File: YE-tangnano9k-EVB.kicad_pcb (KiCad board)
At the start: 2 copper layers, 95 x 72 mm, 27 parts, among them J1 Conn_01x24_Socket, J2 Conn_01x24_Socket, Q1 2SC1815, SW1 SW_SPDT, SW2 SW_Push, SW3 SW_Push, SW4 SW_Push, SW5 SW_Push, SW6 SW_Push, U1 Tang Nano 9K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

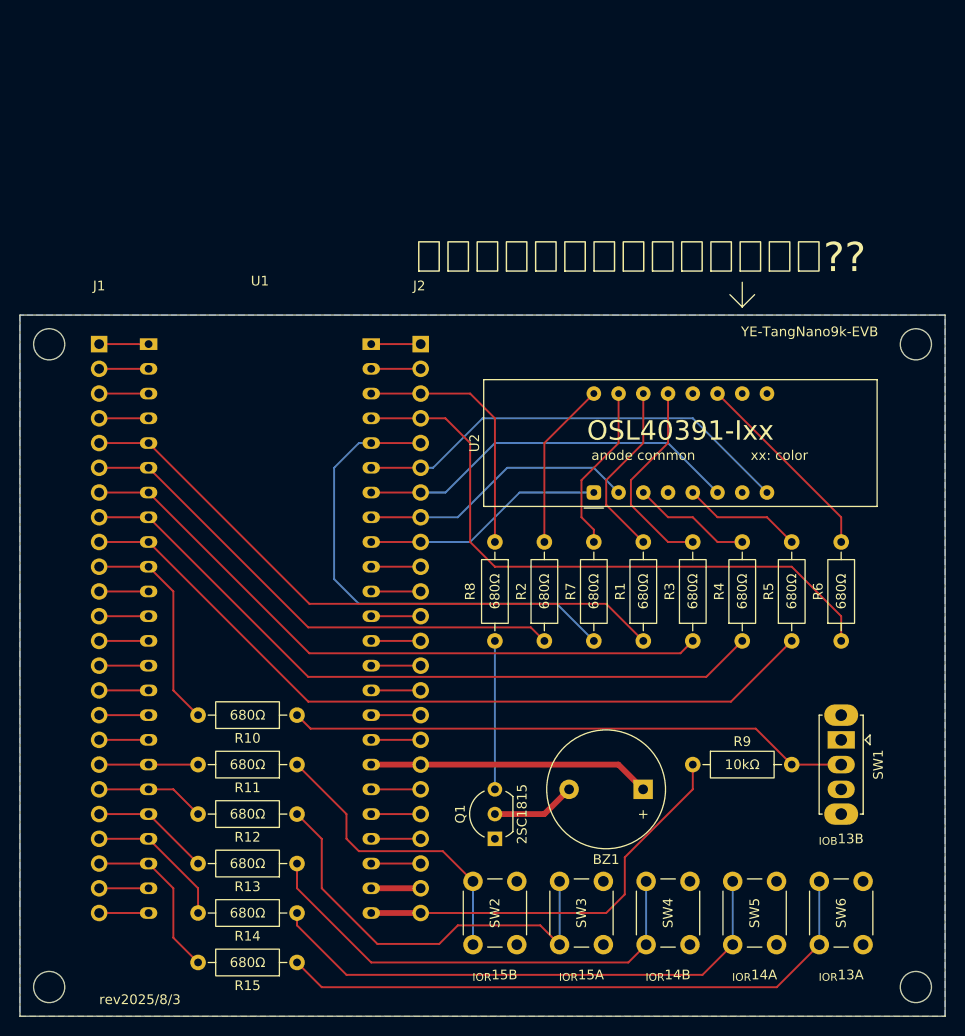
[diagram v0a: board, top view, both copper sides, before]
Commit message: add yasushi_icon fix Front_silk
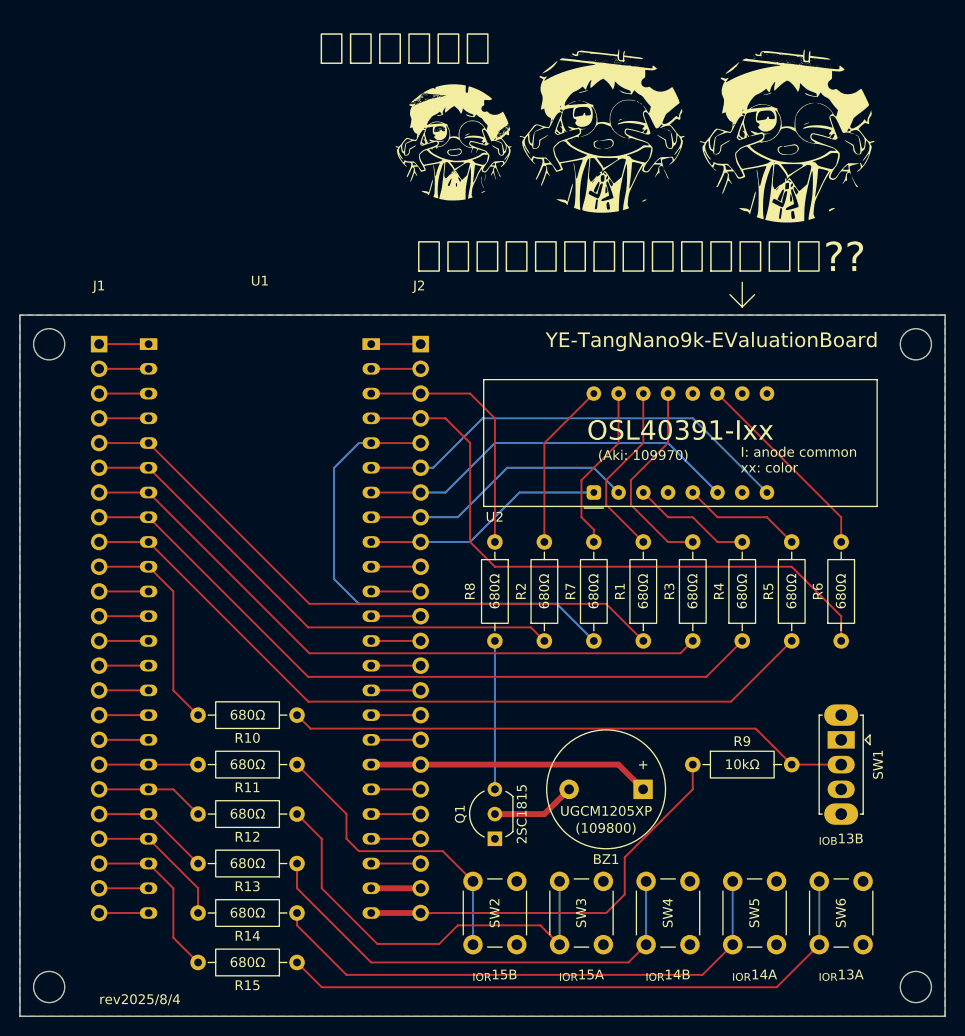
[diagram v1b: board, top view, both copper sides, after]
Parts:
- added G***: LOGO, LOGO, F.Cu at (12.2, -55.0)
- added G***: LOGO, LOGO, F.Cu at (-3.00, -53.8)
- added G***: LOGO, LOGO, F.Cu at (31.2, -54.5)
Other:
- board text added: "(Aki: 109970)"
- board text added: "I: anode common xx: color"
- board text added: "YE-TangNano9k-EValuationBoard"
- board text added: "rev2025/8/4"
- board text added: "アイコン素材"
- board text removed: "YE-TangNano9k-EVB"
- board text removed: "anode common"
- board text removed: "rev2025/8/3"
- board text removed: "xx: color"

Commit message: fix net_name
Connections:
- net /BUZZ renamed /bz
- net /DIG1 renamed /com_1
- net /DIG2 renamed /com_2
- net /DIG3 renamed /com_3
- net /DIG4 renamed /com_4
- net /LED_A renamed /seg_a
- net /LED_B renamed /seg_b
- net /LED_C renamed /seg_c
- net /LED_D renamed /seg_d
- net /LED_E renamed /seg_e
- net /LED_F renamed /seg_f
- net /LED_G renamed /seg_g
- net /Push1 renamed /Push_1
- net /Push2 renamed /Push_2
- net /Push3 renamed /Push_3
- net /Push4 renamed /Push_4
- net /Push5 renamed /Push_5
- net /SW_IN renamed /SYS_EN
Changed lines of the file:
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@@
 	(net 3 "Net-(J1-Pin_15)")
 	(net 4 "Net-(J1-Pin_16)")
-	(net 5 "/Push3")
-	(net 6 "/LED_B")
-	(net 7 "/LED_A")
+	(net 5 "/Push_3")
+	(net 6 "/seg_b")
+	(net 7 "/seg_a")
 	(net 8 "Net-(J1-Pin_13)")
-	(net 9 "/Push1")
+	(net 9 "/Push_1")
 	(net 10 "Net-(J1-Pin_3)")
-	(net 11 "/LED_E")
-	(net 12 "/LED_D")
-	(net 13 "/LED_C")
+	(net 11 "/seg_e")
+	(net 12 "/seg_d")
+	(net 13 "/seg_c")
 	(net 14 "Net-(J1-Pin_14)")
 	(net 15 "Net-(J1-Pin_2)")
 	(net 16 "Net-(J1-Pin_12)")
-	(net 17 "/Push4")
+	(net 17 "/Push_4")
 	(net 18 "Net-(J1-Pin_11)")
-	(net 19 "/Push5")
-	(net 20 "/SW_IN")
+	(net 19 "/Push_5")
+	(net 20 "/SYS_EN")
 	(net 21 "Net-(J1-Pin_17)")
 	(net 22 "Net-(J1-Pin_23)")
-	(net 23 "/Push2")
+	(net 23 "/Push_2")
 	(net 24 "Net-(J1-Pin_24)")
 	(net 25 "Net-(J1-Pin_4)")
@@
 	(net 27 "Net-(J2-Pin_11)")
 	(net 28 "GND")
-	(net 29 "/DIG3")
-	(net 30 "/DIG4")
-	(net 31 "/BUZZ")
+	(net 29 "/com_3")
+	(net 30 "/com_4")
+	(net 31 "/bz")
 	(net 32 "Net-(J2-Pin_21)")
 	(net 33 "Net-(J2-Pin_17)")
 	(net 34 "Net-(J2-Pin_15)")
 	(net 35 "Net-(J2-Pin_12)")
-	(net 36 "/DIG1")
+	(net 36 "/com_1")
 	(net 37 "Net-(J2-Pin_22)")
 	(net 38 "Net-(J2-Pin_2)")
@@
 	(net 41 "+3V3")
 	(net 42 "Net-(J2-Pin_10)")
-	(net 43 "/DIG2")
+	(net 43 "/com_2")
 	(net 44 "Net-(J2-Pin_13)")
-	(net 45 "/LED_F")
+	(net 45 "/seg_f")
 	(net 46 "Net-(J2-Pin_19)")
 	(net 47 "Net-(J2-Pin_16)")
-	(net 48 "/LED_G")
+	(net 48 "/seg_g")
 	(net 49 "Net-(J2-Pin_14)")
 	(net 50 "Net-(Q1-B)")
@@
 			(layers "*.Cu" "*.Mask")
 			(remove_unused_layers no)
-			(net 6 "/LED_B")
+			(net 6 "/seg_b")
 			(pintype "passive")
 		)
@@
 			(layers "*.Cu" "*.Mask")
 			(remove_unused_layers no)
-			(net 31 "/BUZZ")
+			(net 31 "/bz")
 			(pintype "passive")
 		)
@@
 			(layers "*.Cu" "*.Mask")
 			(remove_unused_layers no)
-			(net 20 "/SW_IN")
+			(net 20 "/SYS_EN")
 			(pintype "passive")
 		)
@@
 			(layers "*.Cu" "*.Mask")
 			(remove_unused_layers no)
-			(net 7 "/LED_A")
+			(net 7 "/seg_a")
 			(pintype "passive")
 		)
@@
 			(layers "*.Cu" "*.Mask")
 			(remove_unused_layers no)
-			(net 19 "/Push5")
+			(net 19 "/Push_5")
 			(pintype "passive")
 		)
@@
 			(layers "*.Cu" "*.Mask")
 			(remove_unused_layers no)
-			(net 12 "/LED_D")
+			(net 12 "/seg_d")
 			(pintype "passive")
 		)
@@
 			(layers "*.Cu" "*.Mask")
 			(remove_unused_layers no)
-			(net 45 "/LED_F")
+			(net 45 "/seg_f")
 			(pintype "passive")
 		)
@@
 			(layers "*.Cu" "*.Mask")
 			(remove_unused_layers no)
-			(net 13 "/LED_C")
+			(net 13 "/seg_c")
 			(pintype "passive")
 		)
@@
 			(layers "*.Cu" "*.Mask")
 			(remove_unused_layers no)
-			(net 11 "/LED_E")
+			(net 11 "/seg_e")
 			(pintype "passive")
 		)
@@
 			(layers "*.Cu" "*.Mask")
 			(remove_unused_layers no)
-			(net 23 "/Push2")
+			(net 23 "/Push_2")
 			(pintype "passive")
 		)
@@
 			(layers "*.Cu" "*.Mask")
 			(remove_unused_layers no)
-			(net 7 "/LED_A")
+			(net 7 "/seg_a")
 			(pinfunction "PIN25_IOB8A")
 			(pintype "passive")
@@
 			(layers "*.Cu" "*.Mask")
 			(remove_unused_layers no)
-			(net 6 "/LED_B")
+			(net 6 "/seg_b")
 			(pinfunction "PIN26_IOB8B")
 			(pintype "passive")
@@
 			(layers "*.Cu" "*.Mask")
 			(remove_unused_layers no)
-			(net 13 "/LED_C")
+			(net 13 "/seg_c")
 			(pinfunction "PIN27_IOB11A")
 			(pintype "passive")
@@
 			(layers "*.Cu" "*.Mask")
 			(remove_unused_layers no)
-			(net 12 "/LED_D")
+			(net 12 "/seg_d")
 			(pinfunction "PIN28_IOB11B")
 			(pintype "passive")
@@
 			(layers "*.Cu" "*.Mask")
 			(remove_unused_layers no)
-			(net 11 "/LED_E")
+			(net 11 "/seg_e")
 			(pinfunction "PIN29_IOB13A")
 			(pintype "passive")
@@
 			(layers "*.Cu" "*.Mask")
 			(remove_unused_layers no)
-			(net 20 "/SW_IN")
+			(net 20 "/SYS_EN")
 			(pinfunction "PIN30_IOB13B")
 			(pintype "passive")
@@
 			(layers "*.Cu" "*.Mask")
 			(remove_unused_layers no)
-			(net 9 "/Push1")
+			(net 9 "/Push_1")
 			(pinfunction "PIN53_IOR15B_RGB_B4")
 			(pintype "passive")
@@
 			(layers "*.Cu" "*.Mask")
 			(remove_unused_layers no)
-			(net 23 "/Push2")
+			(net 23 "/Push_2")
 			(pinfunction "PIN54_IOR15A_RGB_B3")
 			(pintype "passive")
@@
 			(layers "*.Cu" "*.Mask")
 			(remove_unused_layers no)
-			(net 5 "/Push3")
+			(net 5 "/Push_3")
 			(pinfunction "PIN55_IOR14B_RGB_G7")
 			(pintype "passive")
@@
 			(layers "*.Cu" "*.Mask")
 			(remove_unused_layers no)
-			(net 17 "/Push4")
+			(net 17 "/Push_4")
 			(pinfunction "PIN56_IOR14A_RGB_G6")
 			(pintype "passive")
@@
 			(layers "*.Cu" "*.Mask")
 			(remove_unused_layers no)
-			(net 19 "/Push5")
+			(net 19 "/Push_5")
 			(pinfunction "PIN57_IOR13A_RGB_G5")
 			(pintype "passive")
@@
 			(layers "*.Cu" "*.Mask")
 			(remove_unused_layers no)
-			(net 36 "/DIG1")
+			(net 36 "/com_1")
 			(pinfunction "PIN79_IOT12B_1V8")
 			(pintype "passive")
@@
 			(layers "*.Cu" "*.Mask")
 			(remove_unused_layers no)
-			(net 43 "/DIG2")
+			(net 43 "/com_2")
 			(pinfunction "PIN80_IOT12A_1V8")
 			(pintype "passive")
@@
 			(layers "*.Cu" "*.Mask")
 			(remove_unused_layers no)
-			(net 29 "/DIG3")
+			(net 29 "/com_3")
 			(pinfunction "PIN81_IOT11B_1V8")
 			(pintype "passive")
@@
 			(layers "*.Cu" "*.Mask")
 			(remove_unused_layers no)
-			(net 30 "/DIG4")
+			(net 30 "/com_4")
 			(pinfunction "PIN82_IOT11A_1V8")
 			(pintype "passive")
@@
 			(layers "*.Cu" "*.Mask")
 			(remove_unused_layers no)
-			(net 48 "/LED_G")
+			(net 48 "/seg_g")
 			(pinfunction "PIN83_IOT10B_1V8")
 			(pintype "passive")
@@
 			(layers "*.Cu" "*.Mask")
 			(remove_unused_layers no)
-			(net 45 "/LED_F")
+			(net 45 "/seg_f")
 			(pinfunction "PIN84_IOT10A_1V8")
 			(pintype "passive")
@@
 			(layers "*.Cu" "*.Mask")
 			(remove_unused_layers no)
-			(net 31 "/BUZZ")
+			(net 31 "/bz")
 			(pinfunction "PIN85_IOT8B_1V8")
 			(pintype "passive")
@@
 			(layers "*.Cu" "*.Mask")
 			(remove_unused_layers no)
-			(net 9 "/Push1")
+			(net 9 "/Push_1")
 			(pintype "passive")
 		)
@@
 			(layers "*.Cu" "*.Mask")
 			(remove_unused_layers no)
-			(net 17 "/Push4")
+			(net 17 "/Push_4")
 			(pintype "passive")
 		)
@@
 			(layers "*.Cu" "*.Mask")
 			(remove_unused_layers no)
-			(net 48 "/LED_G")
+			(net 48 "/seg_g")
 			(pintype "passive")
 		)
@@
 			(layers "*.Cu" "*.Mask")
 			(remove_unused_layers no)
-			(net 7 "/LED_A")
+			(net 7 "/seg_a")
 			(pinfunction "Pin_5")
 			(pintype "passive")
@@
 			(layers "*.Cu" "*.Mask")
 			(remove_unused_layers no)
-			(net 6 "/LED_B")
+			(net 6 "/seg_b")
 			(pinfunction "Pin_6")
 			(pintype "passive")
@@
 			(layers "*.Cu" "*.Mask")
 			(remove_unused_layers no)
-			(net 13 "/LED_C")
+			(net 13 "/seg_c")
 			(pinfunction "Pin_7")
 			(pintype "passive")
@@
 			(layers "*.Cu" "*.Mask")
 			(remove_unused_layers no)
-			(net 12 "/LED_D")
+			(net 12 "/seg_d")
 			(pinfunction "Pin_8")
 			(pintype "passive")
@@
 			(layers "*.Cu" "*.Mask")
 			(remove_unused_layers no)
-			(net 11 "/LED_E")
+			(net 11 "/seg_e")
 			(pinfunction "Pin_9")
 			(pintype "passive")
@@
 			(layers "*.Cu" "*.Mask")
 			(remove_unused_layers no)
-			(net 20 "/SW_IN")
+			(net 20 "/SYS_EN")
 			(pinfunction "Pin_10")
 			(pintype "passive")
@@
 			(layers "*.Cu" "*.Mask")
 			(remove_unused_layers no)
-			(net 9 "/Push1")
+			(net 9 "/Push_1")
 			(pinfunction "Pin_18")
 			(pintype "passive")
@@
 			(layers "*.Cu" "*.Mask")
 			(remove_unused_layers no)
-			(net 23 "/Push2")
+			(net 23 "/Push_2")
 			(pinfunction "Pin_19")
 			(pintype "passive")
@@
 			(layers "*.Cu" "*.Mask")
 			(remove_unused_layers no)
-			(net 5 "/Push3")
+			(net 5 "/Push_3")
 			(pinfunction "Pin_20")
 			(pintype "passive")
@@
 			(layers "*.Cu" "*.Mask")
 			(remove_unused_layers no)
-			(net 17 "/Push4")
+			(net 17 "/Push_4")
 			(pinfunction "Pin_21")
 			(pintype "passive")
@@
 			(layers "*.Cu" "*.Mask")
 			(remove_unused_layers no)
-			(net 19 "/Push5")
+			(net 19 "/Push_5")
 			(pinfunction "Pin_22")
 			(pintype "passive")
@@
 			(remove_unused_layers no)
 			(roundrect_rratio 0.25)
-			(net 36 "/DIG1")
+			(net 36 "/com_1")
 			(pinfunction "CA1")
 			(pintype "input")
@@
 			(layers "*.Cu" "*.Mask")
 			(remove_unused_layers no)
-			(net 43 "/DIG2")
+			(net 43 "/com_2")
 			(pinfunction "CA2")
 			(pintype "input")
@@
 			(layers "*.Cu" "*.Mask")
 			(remove_unused_layers no)
-			(net 29 "/DIG3")
+			(net 29 "/com_3")
 			(pinfunction "CA3")
 			(pintype "input")
@@
 			(layers "*.Cu" "*.Mask")
 			(remove_unused_layers no)
-			(net 30 "/DIG4")
+			(net 30 "/com_4")
 			(pinfunction "CA4")
 			(pintype "input")
@@
 			(layers "*.Cu" "*.Mask")
 			(remove_unused_layers no)
-			(net 5 "/Push3")
+			(net 5 "/Push_3")
 			(pintype "passive")
 		)
@@
 			(layers "*.Cu" "*.Mask")
 			(remove_unused_layers no)
-			(net 31 "/BUZZ")
+			(net 31 "/bz")
 			(pinfunction "Pin_3")
 			(pintype "passive")
@@
 			(layers "*.Cu" "*.Mask")
 			(remove_unused_layers no)
-			(net 45 "/LED_F")
+			(net 45 "/seg_f")
 			(pinfunction "Pin_4")
 			(pintype "passive")
@@
 			(layers "*.Cu" "*.Mask")
 			(remove_unused_layers no)
-			(net 48 "/LED_G")
+			(net 48 "/seg_g")
 			(pinfunction "Pin_5")
 			(pintype "passive")
@@
 			(layers "*.Cu" "*.Mask")
 			(remove_unused_layers no)
-			(net 30 "/DIG4")
+			(net 30 "/com_4")
 			(pinfunction "Pin_6")
 			(pintype "passive")
@@
 			(layers "*.Cu" "*.Mask")
 			(remove_unused_layers no)
-			(net 29 "/DIG3")
+			(net 29 "/com_3")
 			(pinfunction "Pin_7")
 			(pintype "passive")
@@
 			(layers "*.Cu" "*.Mask")
 			(remove_unused_layers no)
-			(net 43 "/DIG2")
+			(net 43 "/com_2")
 			(pinfunction "Pin_8")
 			(pintype "passive")
@@
 			(layers "*.Cu" "*.Mask")
 			(remove_unused_layers no)
-			(net 36 "/DIG1")
+			(net 36 "/com_1")
 			(pinfunction "Pin_9")
 			(pintype "passive")

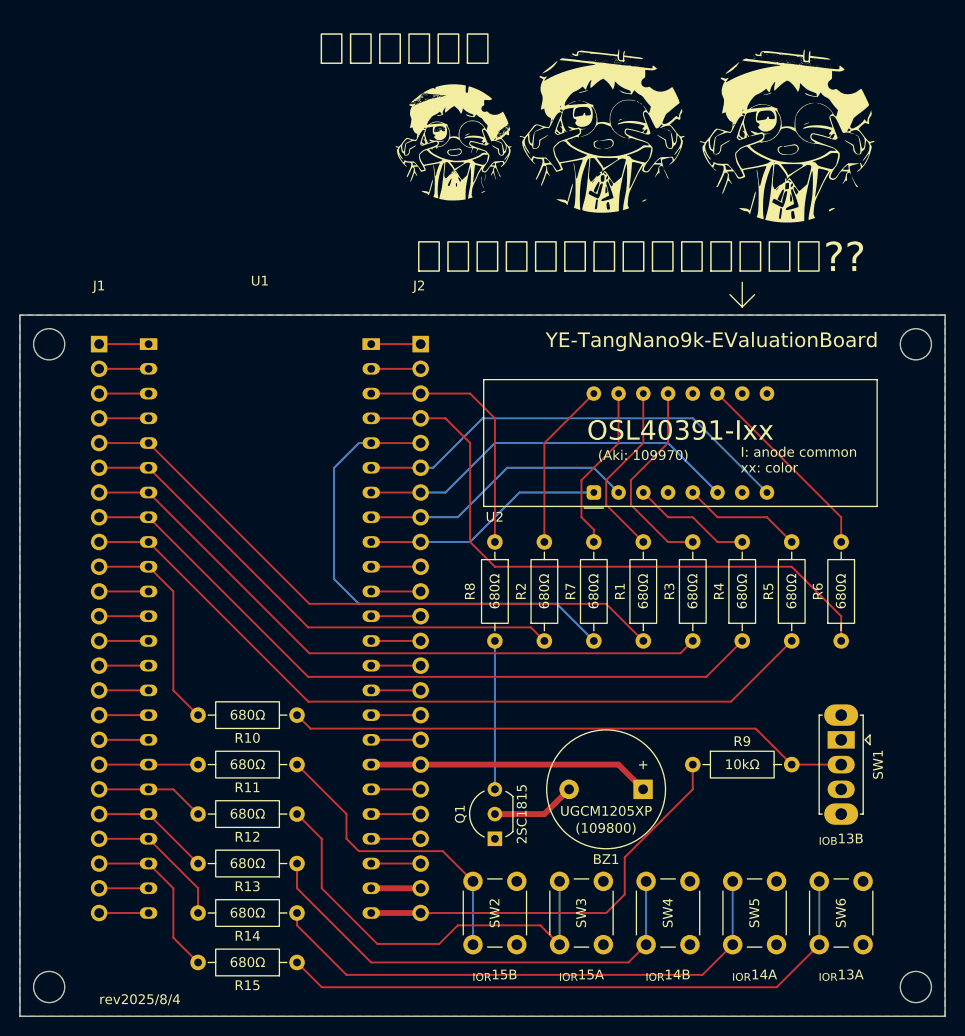
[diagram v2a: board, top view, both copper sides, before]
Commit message: change pushSW net change buzzer logic(ActiveHigh → ActiveLow)
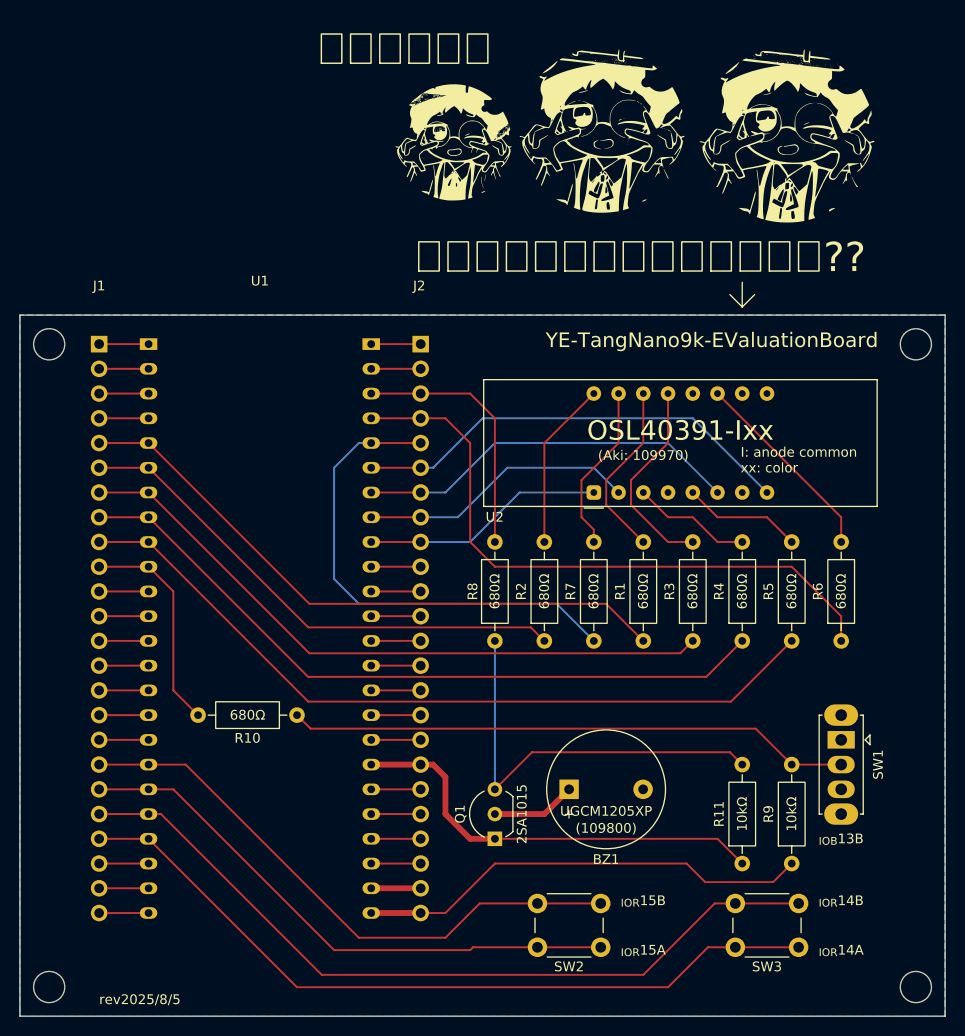
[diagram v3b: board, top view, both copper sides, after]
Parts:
- removed R12, R13, R14, R15: 680, Resistor_THT:R_Axial_DIN0207_L6.3mm_D2.5mm_P10.16mm_Horizontal
- removed SW4, SW5, SW6: SW_Push, Button_Switch_THT:SW_PUSH_6mm_H7.3mm
- Q1: value 2SC1815 -> 2SA1015
- R11: value 680 -> 10k
- moved R11 46.8 mm to (26.7, 20.3), turned to 90 degrees
- moved R9 14.4 mm to (31.8, 20.3), turned to 90 degrees
- moved SW3 13.7 mm to (26.0, 24.4), turned to 0 degrees
- moved R8 10.2 mm to (1.27, -2.54), turned to 90 degrees
- moved BZ1 7.60 mm to (8.89, 12.7), turned to 0 degrees
- moved SW2 3.11 mm to (5.64, 24.4), turned to 0 degrees
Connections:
- net /Push_5 renamed Net-(J1-Pin_22)
- BZ1 pad 1: +5V -> Net-(BZ1-+)
- BZ1 pad 2: Net-(BZ1--) -> GND
- J1 pad 18: /Push_1 -> /IOR15B
- J1 pad 19: /Push_2 -> /IOR15A
- J1 pad 20: /Push_3 -> /IOR14B
- J1 pad 21: /Push_4 -> /IOR14A
- Q1 pad 1: GND -> +5V
- Q1 pad 2: Net-(BZ1--) -> Net-(BZ1-+)
- R11 pad 1: Net-(R11-Pad1) -> +5V
- R11 pad 2: /Push_1 -> Net-(Q1-B)
- R8 pad 1: /bz -> Net-(Q1-B)
- R8 pad 2: Net-(Q1-B) -> /bz
- SW2 pad 1: GND -> /IOR15B
- SW2 pad 2: Net-(R11-Pad1) -> /IOR15A
- SW3 pad 1: GND -> /IOR14B
- SW3 pad 2: Net-(R12-Pad1) -> /IOR14A
- U1 pad 18: /Push_1 -> /IOR15B
- U1 pad 19: /Push_2 -> /IOR15A
- U1 pad 20: /Push_3 -> /IOR14B
- U1 pad 21: /Push_4 -> /IOR14A
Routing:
- net /IOR14B: track 0.00 -> 81.7 mm
- net /IOR14A: track 0.00 -> 79.8 mm
- net Net-(R15-Pad1): track 63.0 -> 0.00 mm
- net /IOR15B: track 0.00 -> 60.3 mm
- net /IOR15A: track 0.00 -> 58.5 mm
- net Net-(R14-Pad1): track 55.9 -> 0.00 mm
- net Net-(R13-Pad1): track 48.8 -> 0.00 mm
- net Net-(R12-Pad1): track 43.6 -> 0.00 mm
- net Net-(R11-Pad1): track 31.0 -> 0.00 mm
- net Net-(Q1-B): track 15.2 -> 42.7 mm
- net +5V: track 29.0 -> 44.5 mm
- net /Push_4: track 14.8 -> 0.00 mm
- net Net-(J1-Pin_22): track 17.3 -> 5.08 mm
- net /Push_3: track 12.3 -> 0.00 mm
- net /Push_2: track 11.2 -> 0.00 mm
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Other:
- board text added: "rev2025/8/5"
- board text removed: "_{IOR}13A"
- board text removed: "rev2025/8/4"
